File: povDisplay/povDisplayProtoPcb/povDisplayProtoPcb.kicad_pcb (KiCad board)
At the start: 4 copper layers, 41 parts, among them J5 Conn_02x06_Odd_Even

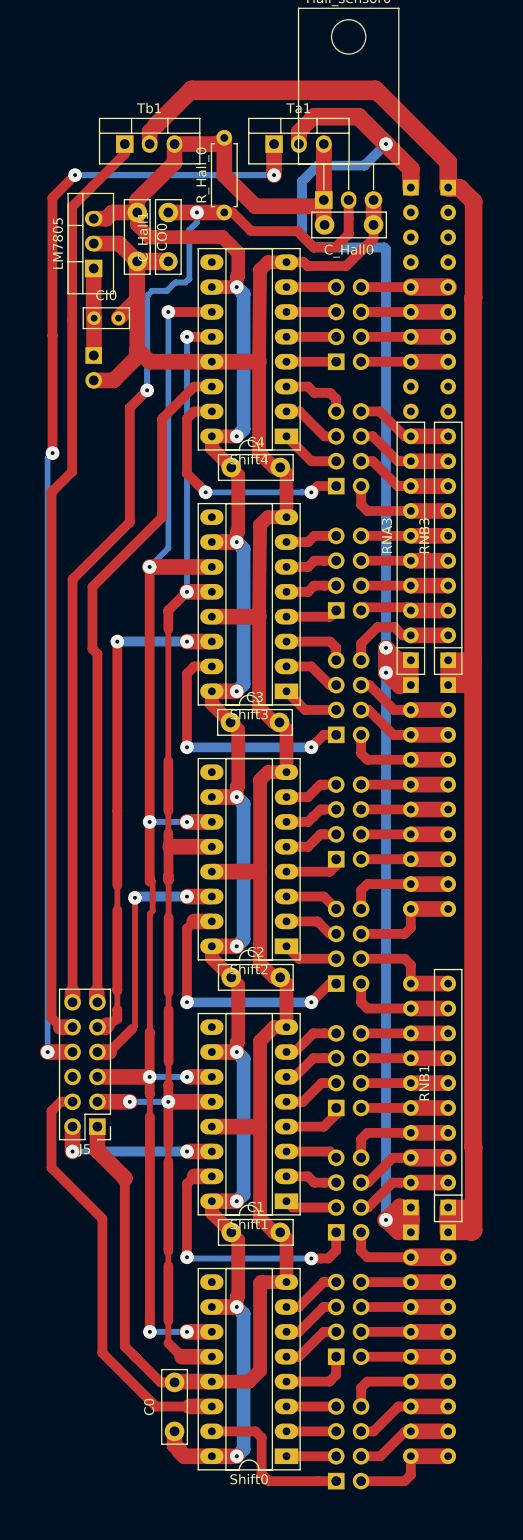
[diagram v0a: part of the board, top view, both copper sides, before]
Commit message: Add cutting edge.
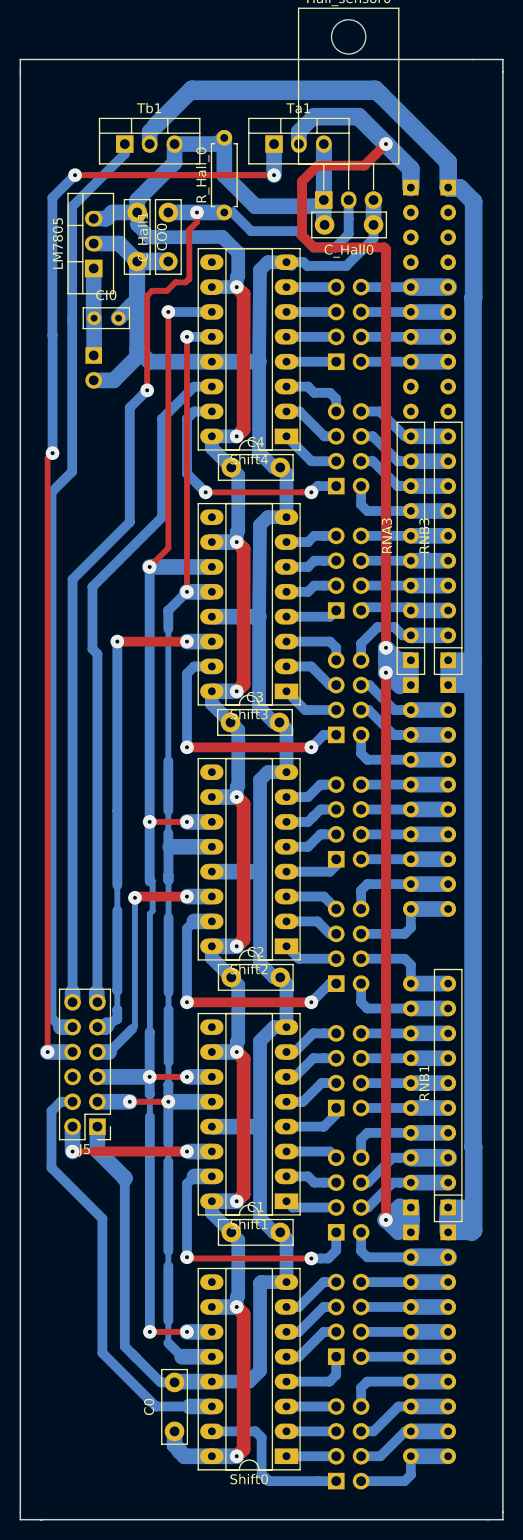
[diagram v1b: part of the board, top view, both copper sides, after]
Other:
- board outline added: 49.3 x 149.1 mm

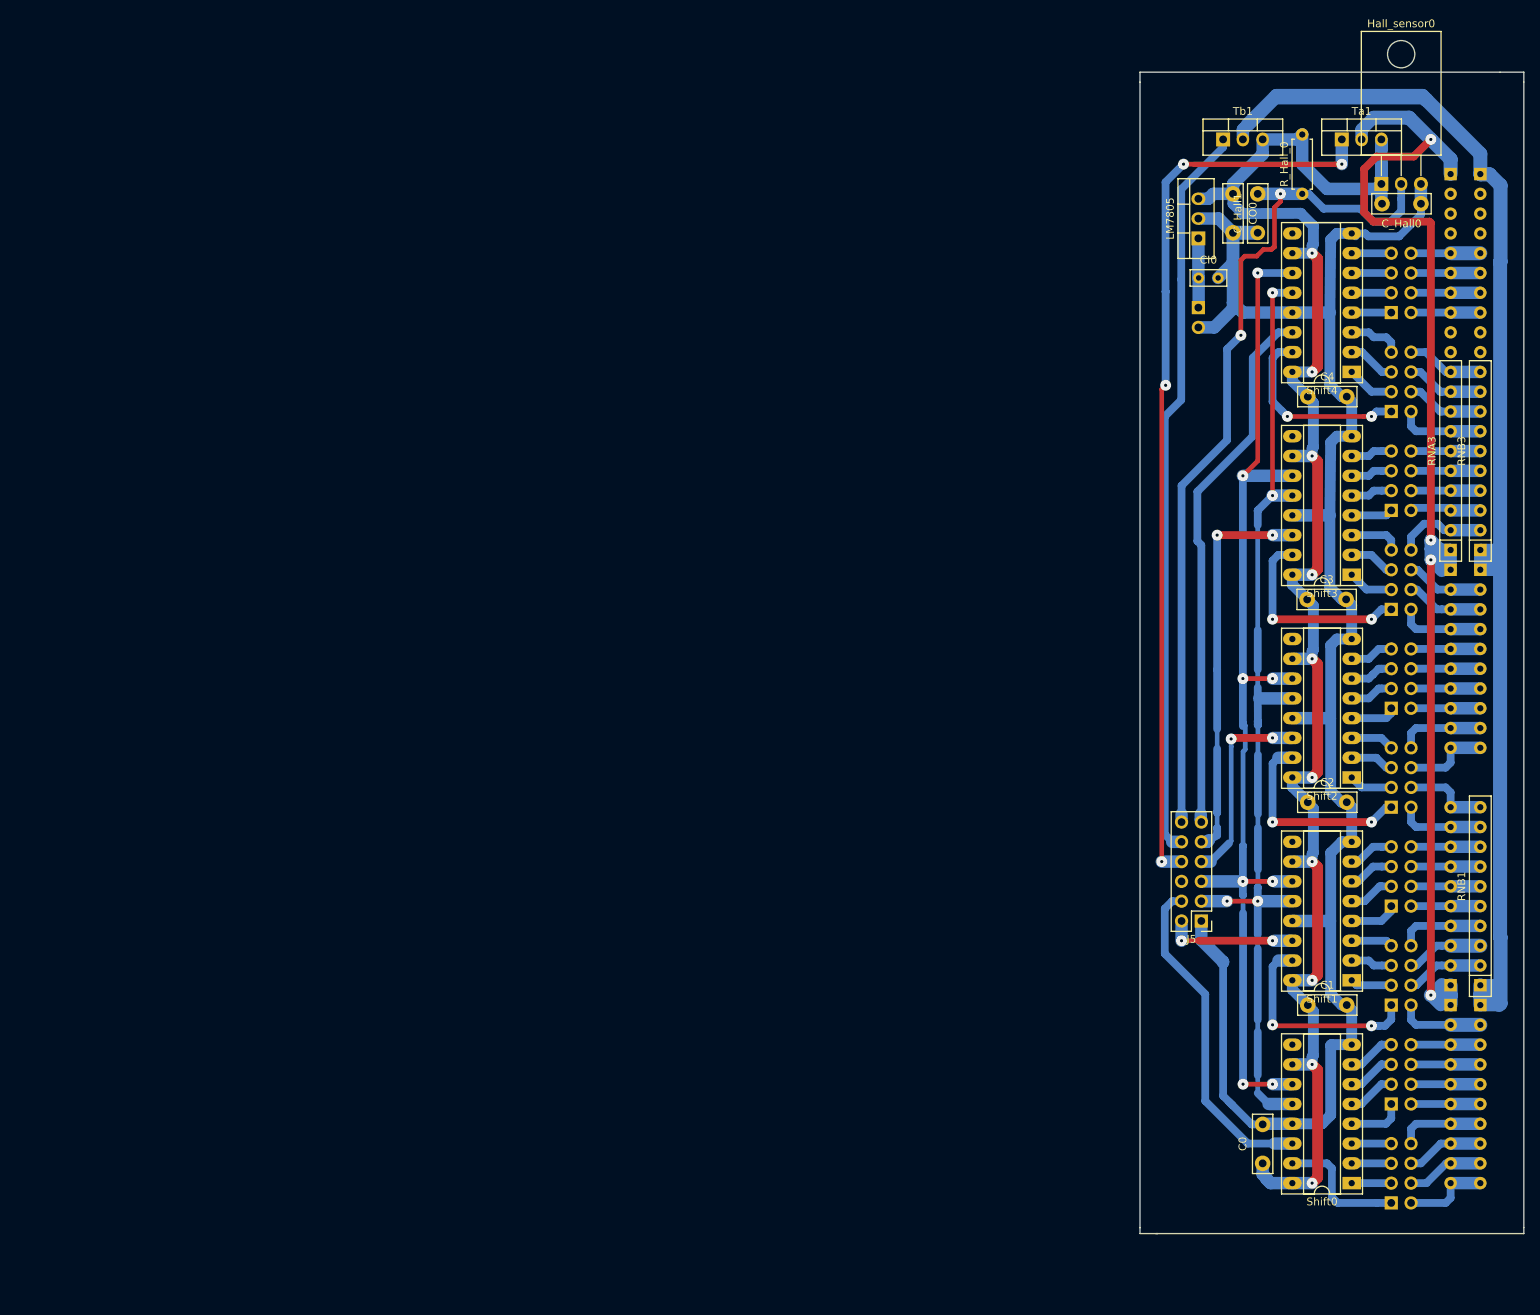
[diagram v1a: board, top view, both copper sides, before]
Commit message: Add mounting holes
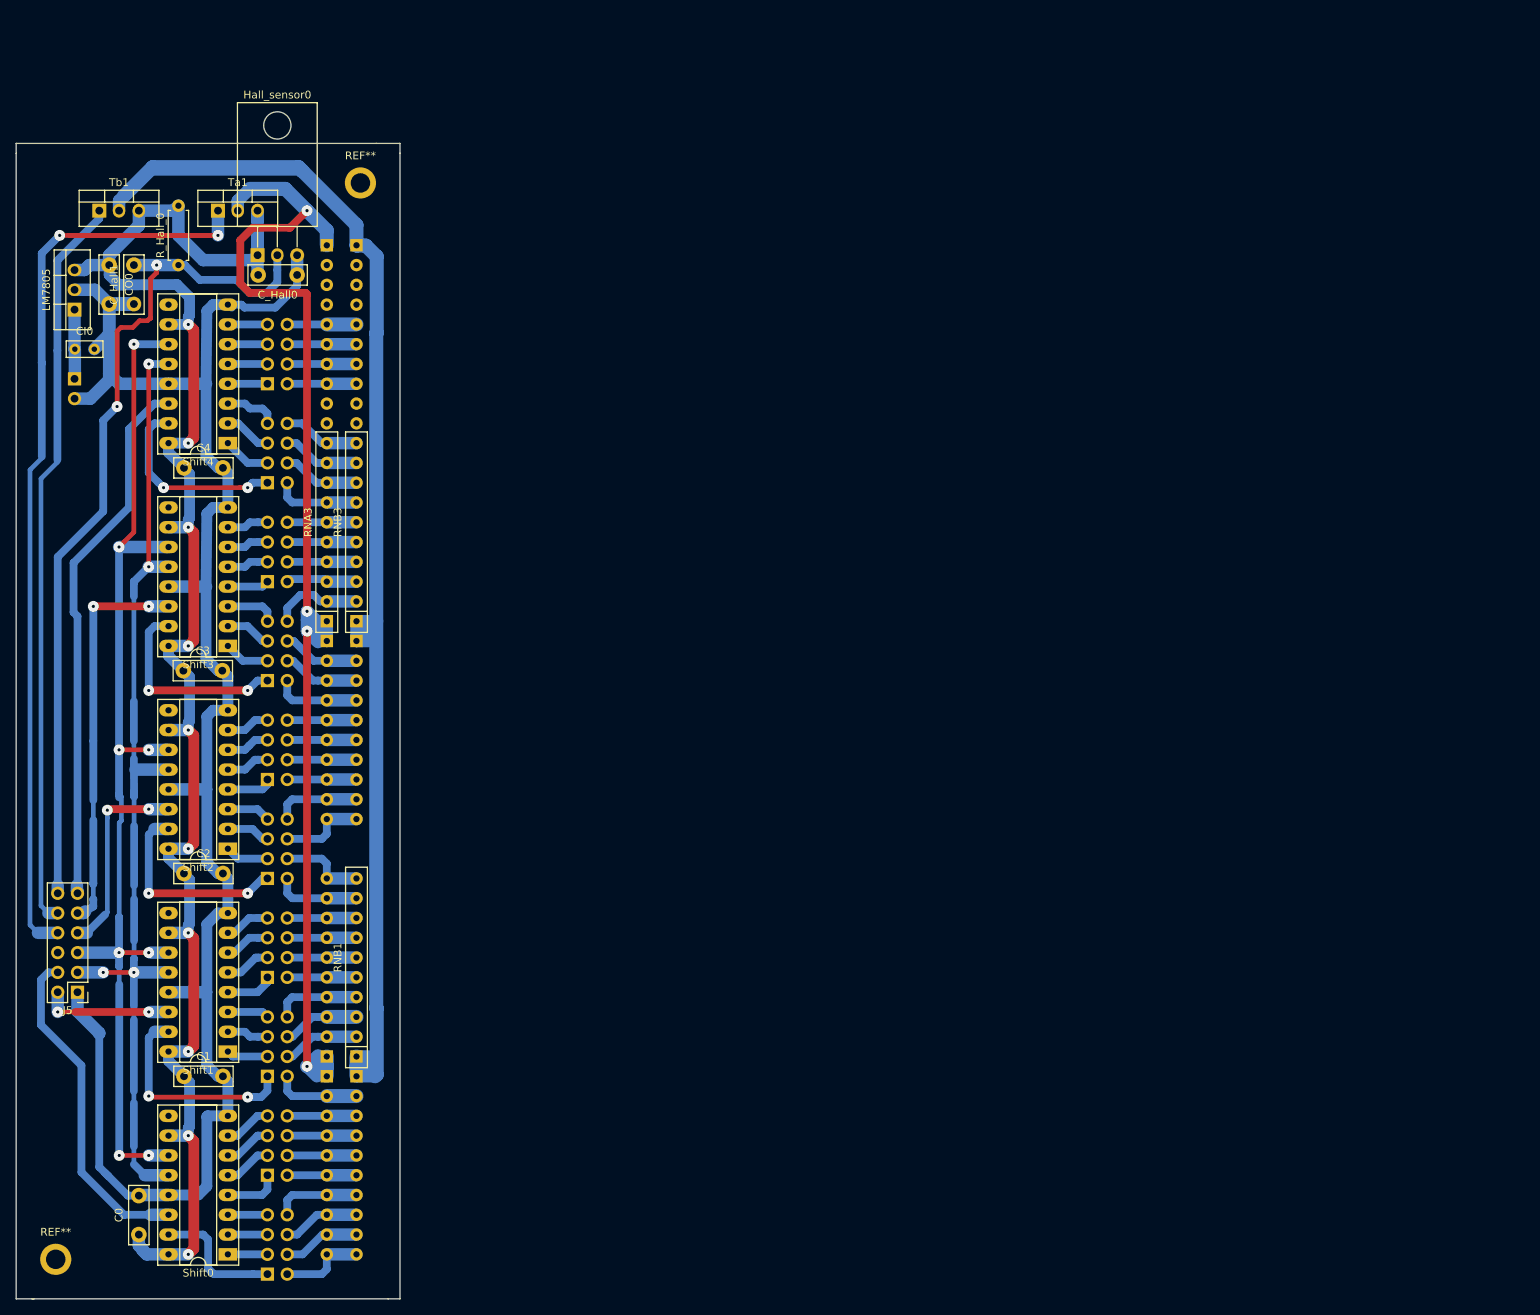
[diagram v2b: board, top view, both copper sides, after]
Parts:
- added REF**: MountingHole_2.5mm_Pad, Mounting_Holes:MountingHole_2.5mm_Pad, F.Cu at (74.7, 29.7)
- added REF**: MountingHole_2.5mm_Pad, Mounting_Holes:MountingHole_2.5mm_Pad, F.Cu at (35.6, 167.9)
- moved R_Hall_0 144.6 mm to (51.3, 40.3)
- moved Bat0 144.6 mm to (38.0, 54.9)
- moved C0 144.6 mm to (46.2, 164.7)
- moved C1 144.6 mm to (52.0, 144.4)
- moved C2 144.6 mm to (52.0, 118.4)
- moved C3 144.6 mm to (51.9, 92.3)
- moved C4 144.6 mm to (52.0, 66.3)
- moved CI0 144.6 mm to (38.0, 51.1)
- moved CO0 144.6 mm to (42.4, 40.3)
- moved C_Hall0 144.6 mm to (66.5, 41.5)
- moved C_Hall1 144.6 mm to (45.6, 45.3)
- moved Hall_sensor0 144.6 mm to (61.5, 39.0)
- moved J5 144.6 mm to (38.4, 133.6)
- moved LM7805 144.6 mm to (38.0, 46.0)
- moved Led00 144.6 mm to (62.7, 169.8)
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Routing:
- net Command_TA: track 135.8 -> 136.6 mm, vias 4 -> 2
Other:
- board size 49.3 x 149.1 mm -> 49.3 x 148.3 mm
